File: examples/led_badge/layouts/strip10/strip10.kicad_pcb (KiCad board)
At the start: 2 copper layers, 20 parts

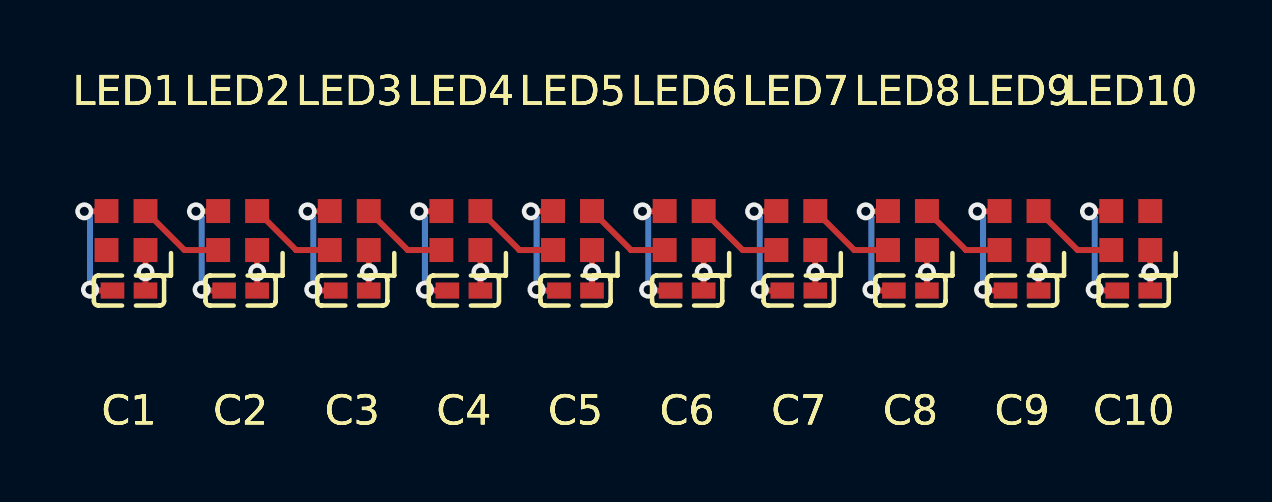
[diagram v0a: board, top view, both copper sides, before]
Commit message: fix 3d models
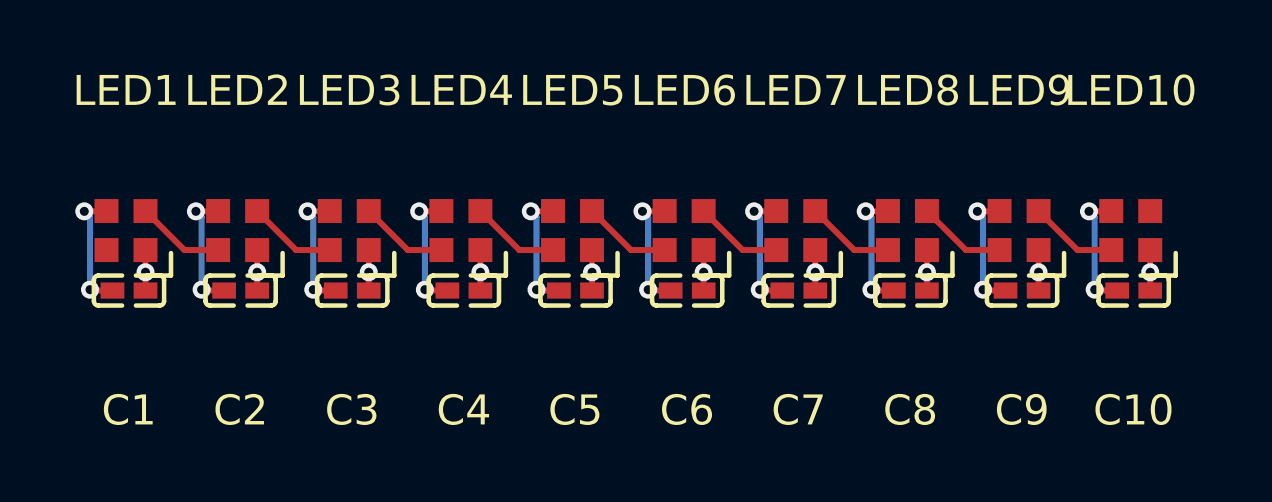
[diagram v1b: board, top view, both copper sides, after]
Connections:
- net DOUT renamed -DOUT-0
- net DOUT-1 renamed -DOUT-1
- net DOUT-2 renamed -DOUT-2
- net DOUT-3 renamed -DOUT-3
- net DOUT-4 renamed -DOUT-4
- net DOUT-5 renamed -DOUT-5
- net DOUT-6 renamed -DOUT-6
- net DOUT-7 renamed -DOUT-7
- net DOUT-8 renamed -DOUT-8
- net DOUT-9 renamed -DOUT-9

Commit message: rebuild lad badge
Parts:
- C1, C10, C2, C3, C4, C5, C6, C7, C8, C9: value 100nF ±10% 16V X7R -> 100nF ±10% 50V X7R; footprint Samsung_Electro_Mechanics_CL05B104KO5NNNC:C0402 -> Samsung_Electro_Mechanics_CL05B104KB54PNC:C0402
- moved C1 96.4 mm to (61.0, 46.2)
- moved C4 96.4 mm to (72.1, 46.2)
- moved C5 96.4 mm to (75.9, 46.2)
- moved C8 96.4 mm to (87.0, 46.2)
- moved C9 96.4 mm to (90.8, 46.2)
- moved LED3 96.4 mm to (68.3, 44.2)
- moved LED4 96.4 mm to (72.0, 44.2)
- moved LED7 96.4 mm to (83.2, 44.2)
- moved LED8 96.4 mm to (86.9, 44.2)
- moved C10 96.4 mm to (94.5, 46.2)
- moved C2 96.4 mm to (64.7, 46.2)
- moved C3 96.4 mm to (68.4, 46.2)
- moved C6 96.4 mm to (79.6, 46.2)
- moved C7 96.4 mm to (83.3, 46.2)
- moved LED1 96.4 mm to (60.9, 44.2)
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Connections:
- net -DOUT-0 renamed DOUT
- net -DOUT-1 renamed leds[1]-data_in-DIN
- net -DOUT-2 renamed leds[2]-data_in-DIN
- net -DOUT-3 renamed leds[3]-data_in-DIN
- net -DOUT-4 renamed leds[4]-data_in-DIN
- net -DOUT-5 renamed leds[5]-data_in-DIN
- net -DOUT-6 renamed leds[6]-data_in-DIN
- net -DOUT-7 renamed leds[7]-data_in-DIN
- net -DOUT-8 renamed leds[8]-data_in-DIN
- net -DOUT-9 renamed leds[9]-data_in-DIN
- net DIN renamed leds[0]-data_in-DIN
- net gnd renamed GND
- net hv renamed VCC

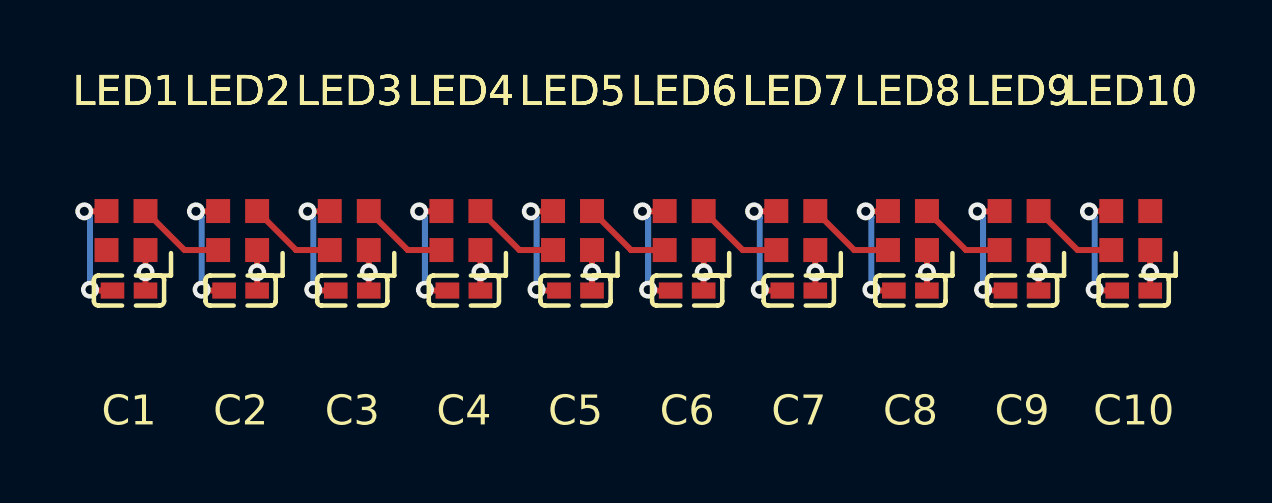
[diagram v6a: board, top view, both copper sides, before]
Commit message: fix import and layout led badge (badge target still fails)
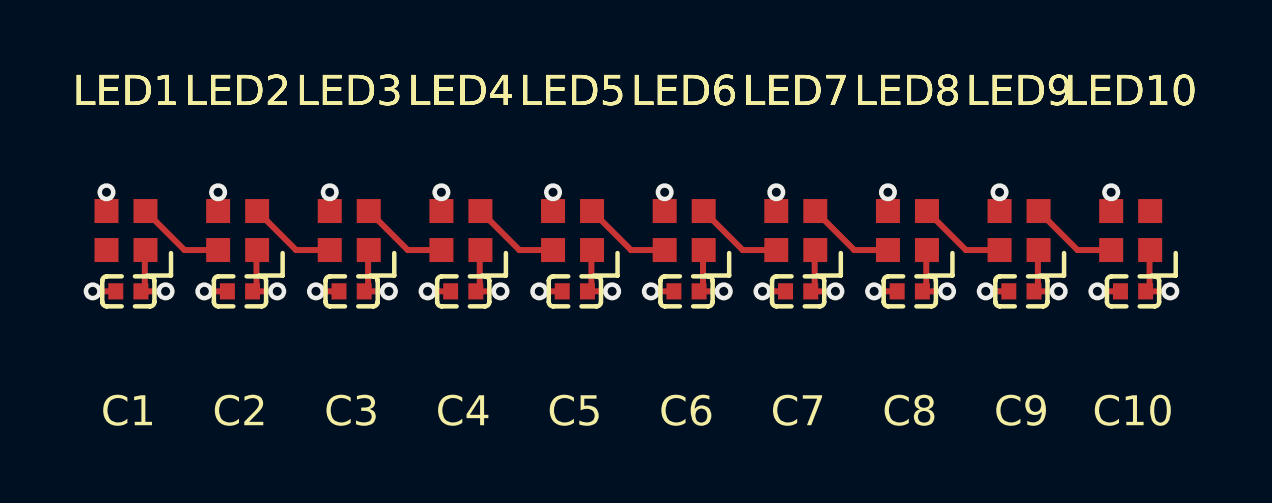
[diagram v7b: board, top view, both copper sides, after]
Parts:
- C1, C10, C2, C3, C4, C5, C6, C7, C8, C9: value 100nF ±10% 50V X7R -> 0F; footprint Samsung_Electro_Mechanics_CL05B104KB54PNC:C0402 -> Samsung_Electro_Mechanics_CL05B104KO5NNNC:C0402
- LED1, LED10, LED2, LED3, LED4, LED5, LED6, LED7, LED8, LED9: footprint OPSCO_SK6805_EC20:LED-SMD_4P-L2.0-W2.0-BR -> OPSCO_Optoelectronics_SK6805_EC20:LED-SMD_4P-L2.0-W2.0-BR
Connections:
- net GND renamed lv
- net VCC renamed hv
- net leds[0]-data_in-DIN renamed DIN
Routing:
- net lv: track 42.0 -> 12.6 mm
- net hv: track 13.5 -> 20.8 mm

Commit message: fix led badge strip/grid builds
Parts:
- C1, C10, C2, C3, C4, C5, C6, C7, C8, C9: value 0F -> 100nF
